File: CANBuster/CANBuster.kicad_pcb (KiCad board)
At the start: 2 copper layers, 100 x 100 mm, 182 parts, among them CON1 BARREL_JACK, J1 RJ45, J2 RJ45, J3 RJ12, P1 CONN_01X10, P10 CONN_02X04, P11 RS232-Programmer, P12 S88, P13 CONN_01X10, P14 CONN_01X10, P15 TRACK, P16 CONN_01X02, P17 USB_OTG, P18 CONN_01X03, P2 CONN_01X10, P3 CONN_01X03, P4 CONN_01X03, P5 CONN_01X03, P6 CONN_01X03, P7 CONN_01X02, P8 CONN_01X06, P9 CONN_01X04, Q1 BC547, Q2 BC547, SW1 SW_PUSH, SW2 SW_PUSH, U1 PIC18F45K80, U12 MCP2561, U2 MCP2561, U3 7805, U4 LTV-844, U5 LTV-844, U6 LTV-844, U7 LTV-844, U8 ISO1050, Y1 16MHz

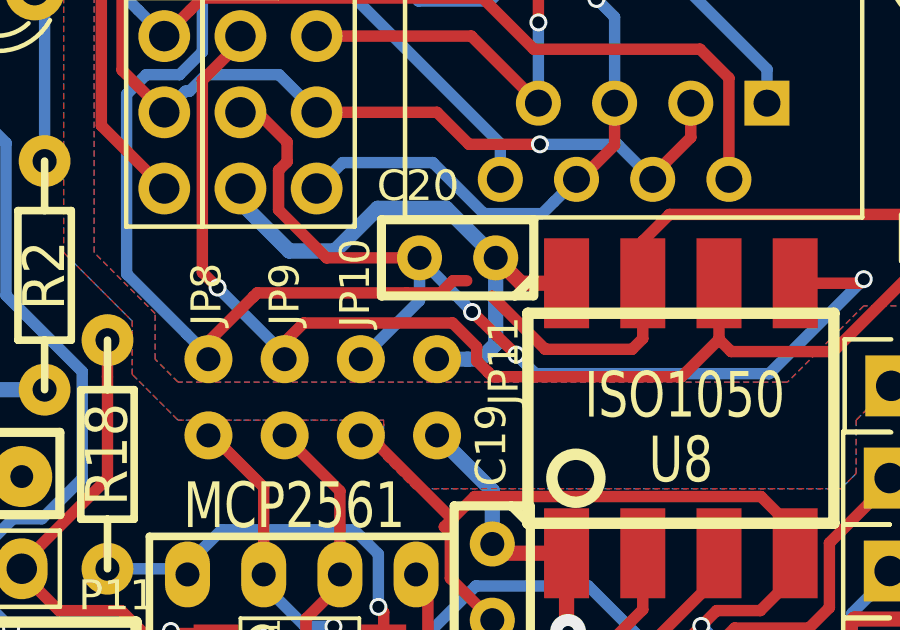
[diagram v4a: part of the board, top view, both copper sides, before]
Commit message: finish 5V option
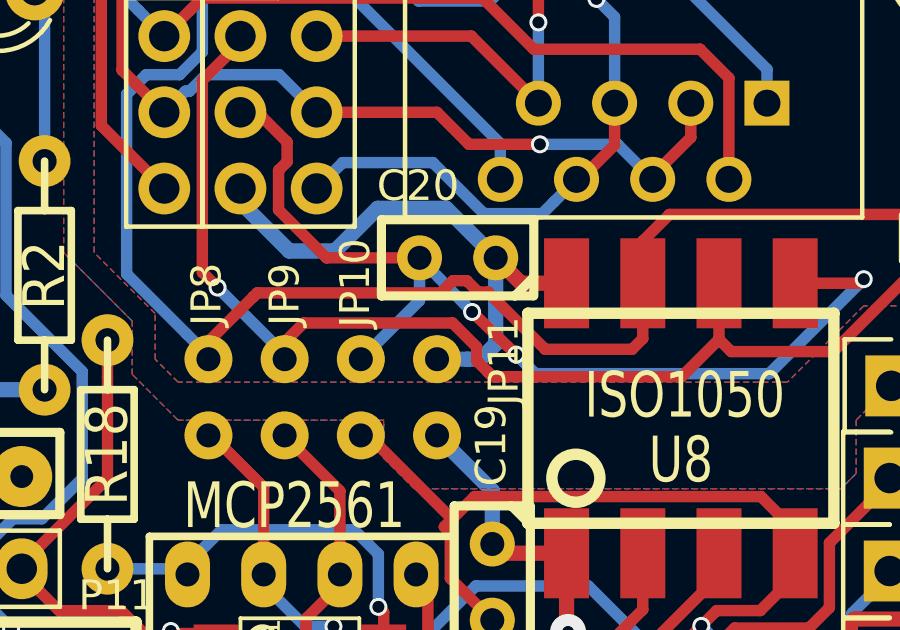
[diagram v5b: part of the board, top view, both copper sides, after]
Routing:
- net /CANH: track 46.3 -> 47.4 mm
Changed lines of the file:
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@@
-(kicad_pcb (version 4) (host pcbnew 4.0.2-4+6225~38~ubuntu14.04.1-stable)
+(kicad_pcb (version 4) (host pcbnew 4.0.1-stable)
   (general
     (links 463)
-    (no_connects 36)
-    (area 70.028999 35.052999 170.179001 135.203001)
+    (no_connects 0)
+    (area 69.215499 29.4545 181.99 144.85554)
     (thickness 1.6)
     (drawings 32)
-    (tracks 1756)
+    (tracks 1755)
     (zones 0)
     (modules 182)
@@
   (segment (start 157.6324 53.086) (end 157.226 52.6796) (width 0.381) (layer F.Cu) (net 36))
   (segment (start 157.226 52.6796) (end 157.226 50.8085) (width 0.381) (layer F.Cu) (net 36))
-  (segment (start 146.812 51.1302) (end 141.8336 51.1302) (width 0.381) (layer F.Cu) (net 37))
-  (segment (start 146.812 51.1302) (end 147.955 51.1302) (width 0.381) (layer F.Cu) (net 37))
-  (segment (start 148.3614 50.7238) (end 147.955 51.1302) (width 0.381) (layer F.Cu) (net 37))
   (segment (start 141.7066 51.2572) (end 141.8336 51.1302) (width 0.381) (layer F.Cu) (net 37))
   (segment (start 148.3614 50.7238) (end 148.8186 50.7238) (width 0.381) (layer F.Cu) (net 37))
-  (segment (start 149.6695 51.2445) (end 149.6441 51.2445) (width 0.381) (layer F.Cu) (net 37))
-  (segment (start 151.4348 53.0098) (end 149.6695 51.2445) (width 0.381) (layer F.Cu) (net 37))
-  (segment (start 154.686 50.8085) (end 154.686 52.6542) (width 0.381) (layer F.Cu) (net 37))
+  (segment (start 149.197671 51.102871) (end 149.527871 51.102871) (width 0.381) (layer F.Cu) (net 37))
+  (segment (start 141.8336 51.1302) (end 147.955 51.1302) (width 0.381) (layer F.Cu) (net 37))
+  (segment (start 149.527871 51.102871) (end 151.4348 53.0098) (width 0.381) (layer F.Cu) (net 37))
+  (segment (start 147.955 51.1302) (end 148.3614 50.7238) (width 0.381) (layer F.Cu) (net 37))
+  (segment (start 148.8186 50.7238) (end 149.197671 51.102871) (width 0.381) (layer F.Cu) (net 37))
+  (segment (start 151.4348 53.0098) (end 154.3304 53.0098) (width 0.381) (layer F.Cu) (net 37))
   (segment (start 154.3304 53.0098) (end 154.686 52.6542) (width 0.381) (layer F.Cu) (net 37))
-  (segment (start 151.4983 53.0098) (end 154.3304 53.0098) (width 0.381) (layer F.Cu) (net 37))
-  (segment (start 151.4983 53.0098) (end 151.4348 53.0098) (width 0.381) (layer F.Cu) (net 37))
+  (segment (start 154.686 52.6542) (end 154.686 50.8085) (width 0.381) (layer F.Cu) (net 37))
   (segment (start 140.2842 52.6796) (end 141.7066 51.2572) (width 0.381) (layer F.Cu) (net 37))
   (segment (start 141.7066 51.2572) (end 141.7193 51.2572) (width 0.381) (layer F.Cu) (net 37))
@@
   (segment (start 150.4696 53.1876) (end 148.9964 51.7652) (width 0.381) (layer F.Cu) (net 151))
   (via (at 148.9964 51.7652) (size 0.6) (drill 0.4) (layers F.Cu B.Cu) (net 151))
-  (segment (start 147.2438 49.9618) (end 148.9964 51.7652) (width 0.381) (layer B.Cu) (net 151) (status 400000))
+  (segment (start 147.2438 49.9618) (end 148.9964 51.7652) (width 0.381) (layer B.Cu) (net 151))
   (segment (start 151.0284 53.7464) (end 150.4696 53.1876) (width 0.381) (layer B.Cu) (net 151))
   (via (at 150.4696 53.1876) (size 0.6) (drill 0.4) (layers F.Cu B.Cu) (net 151))
@@
     (connect_pads (clearance 0.254))
     (min_thickness 0.254)
-    (fill (arc_segments 16) (thermal_gap 0.508) (thermal_bridge_width 0.508))
+    (fill yes (arc_segments 16) (thermal_gap 0.508) (thermal_bridge_width 0.508))
     (polygon
       (pts
@@
     (connect_pads (clearance 0.254))
     (min_thickness 0.254)
-    (fill (arc_segments 16) (thermal_gap 0.508) (thermal_bridge_width 0.508))
+    (fill yes (arc_segments 16) (thermal_gap 0.508) (thermal_bridge_width 0.508))
     (polygon
       (pts
@@
     (connect_pads (clearance 0.254))
     (min_thickness 0.254)
-    (fill (arc_segments 16) (thermal_gap 0.508) (thermal_bridge_width 0.508))
+    (fill yes (arc_segments 16) (thermal_gap 0.508) (thermal_bridge_width 0.508))
     (polygon
       (pts
@@
     (connect_pads (clearance 0.254))
     (min_thickness 0.254)
-    (fill (arc_segments 16) (thermal_gap 0.508) (thermal_bridge_width 0.508))
+    (fill yes (arc_segments 16) (thermal_gap 0.508) (thermal_bridge_width 0.508))
     (polygon
       (pts
@@
     (connect_pads (clearance 0.254))
     (min_thickness 0.254)
-    (fill (arc_segments 16) (thermal_gap 0.508) (thermal_bridge_width 0.508))
+    (fill yes (arc_segments 16) (thermal_gap 0.508) (thermal_bridge_width 0.508))
     (polygon
       (pts
@@
     (connect_pads (clearance 0.254))
     (min_thickness 0.254)
-    (fill (arc_segments 16) (thermal_gap 0.508) (thermal_bridge_width 0.508))
+    (fill yes (arc_segments 16) (thermal_gap 0.508) (thermal_bridge_width 0.508))
     (polygon
       (pts
@@
     (connect_pads (clearance 0.254))
     (min_thickness 0.254)
-    (fill (arc_segments 16) (thermal_gap 0.508) (thermal_bridge_width 0.508))
+    (fill yes (arc_segments 16) (thermal_gap 0.508) (thermal_bridge_width 0.508))
     (polygon
       (pts
@@
     (connect_pads (clearance 0.254))
     (min_thickness 0.254)
-    (fill (arc_segments 16) (thermal_gap 0.508) (thermal_bridge_width 0.508))
+    (fill yes (arc_segments 16) (thermal_gap 0.508) (thermal_bridge_width 0.508))
     (polygon
       (pts

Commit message: bump version
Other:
- board text added: "CANBuster v1.2 4/2016 Gerhard Bertelsmann"
- board text removed: "CANBuster v1.1 3/2016 Gerhard Bertelsmann"
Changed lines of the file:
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@@
-(kicad_pcb (version 4) (host pcbnew 4.0.1-stable)
+(kicad_pcb (version 4) (host pcbnew 4.0.2-4+6225~38~ubuntu14.04.1-stable)
   (general
     (links 463)
@@
     (effects (font (size 1.2 1.2) (thickness 0.2)))
   )
-  (gr_text "CANBuster v1.1 3/2016\nGerhard Bertelsmann" (at 153.289 127.889) (layer F.Cu)
+  (gr_text "CANBuster v1.2 4/2016\nGerhard Bertelsmann" (at 153.289 127.889) (layer F.Cu)
     (effects (font (size 1.2 1.2) (thickness 0.25)))
   )

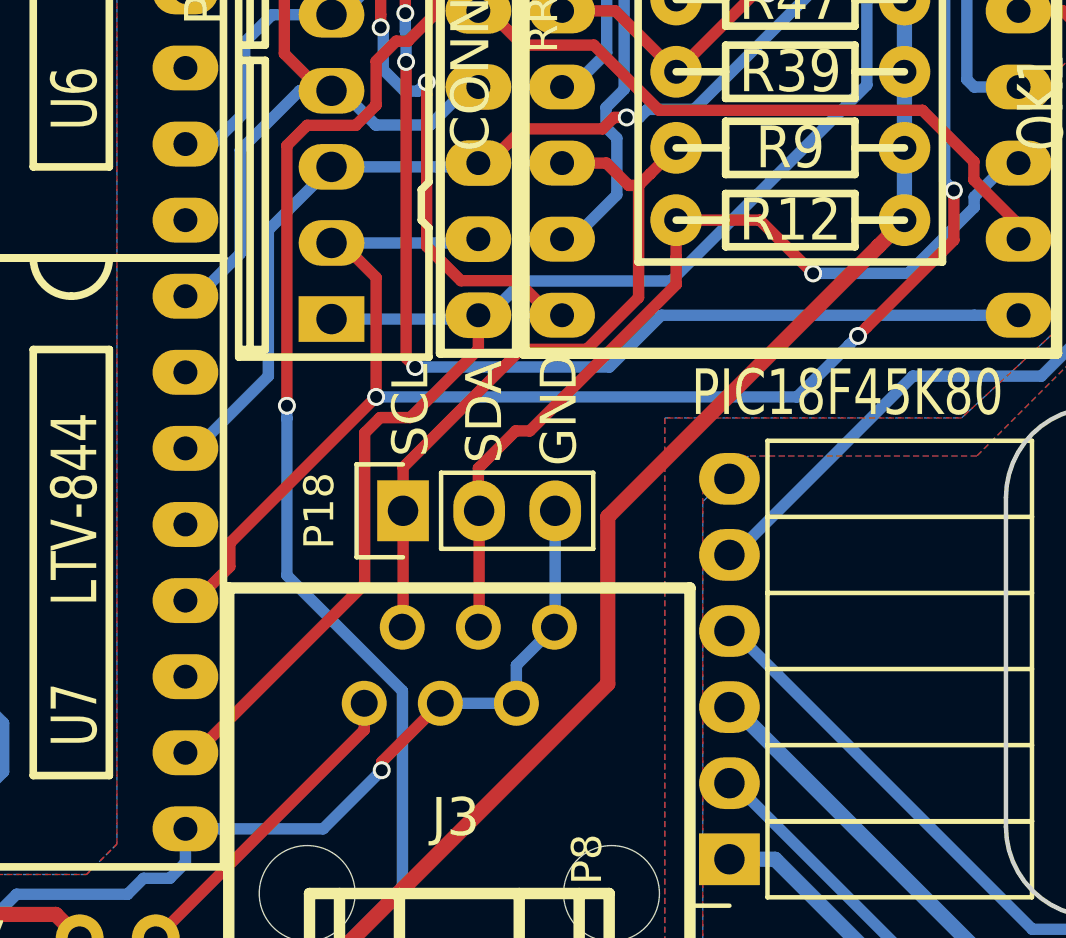
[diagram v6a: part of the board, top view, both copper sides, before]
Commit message: replace IIC 3 pin header with 4 pin - including Vdd
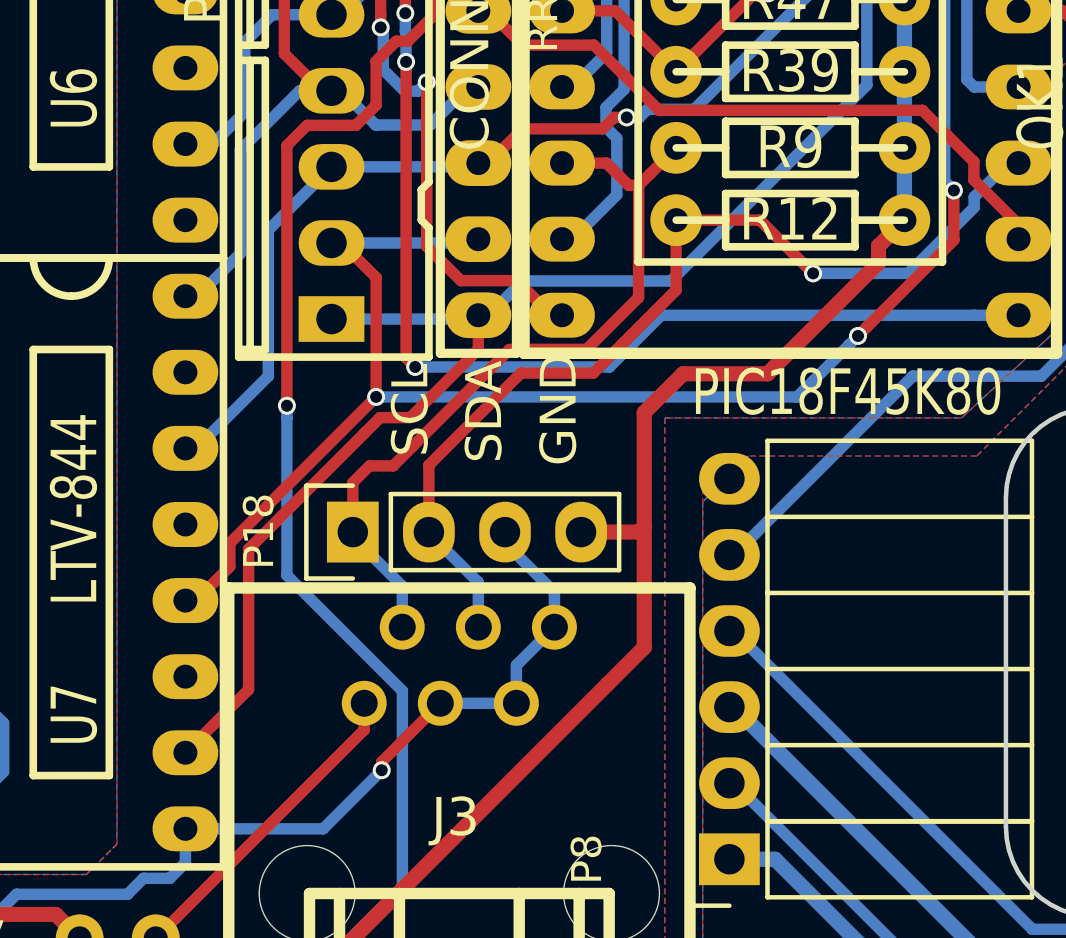
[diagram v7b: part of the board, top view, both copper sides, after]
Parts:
- P18: value CONN_01X03 -> CONN_01X04; footprint Pin_Headers:Pin_Header_Straight_1x03 -> Pin_Headers:Pin_Header_Straight_1x04
- moved P18 1.82 mm to (114.3, 118.9)
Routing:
- net VDD: track 333.7 -> 337.5 mm
- net /SDA: track 30.5 -> 33.0 mm
- net /SCL: track 23.9 -> 26.0 mm

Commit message: wip
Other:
- board text added: "CTS"
- board text added: "DTR"
- board text added: "RxD"
- board text added: "TxD"
- board text added: "Vcc"
- board text added: "Vdd"
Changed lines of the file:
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@@
-(kicad_pcb (version 4) (host pcbnew 4.0.2-4+6225~38~ubuntu14.04.1-stable)
+(kicad_pcb (version 4) (host pcbnew 4.0.1-stable)
   (general
     (links 464)
@@
     (area 70.028999 35.052999 170.179001 135.203001)
     (thickness 1.6)
-    (drawings 32)
+    (drawings 39)
     (tracks 1769)
     (zones 0)
@@
     )
   )
-  (gr_text GND (at 121.1834 114.7826 90) (layer F.SilkS)
+  (gr_text DTR (at 132.08 117.221) (layer F.SilkS)
     (effects (font (size 1.2 1.2) (thickness 0.2)))
   )
-  (gr_text SCL (at 116.2304 114.808 90) (layer F.SilkS)
+  (gr_text RxD (at 132.08 119.761) (layer F.SilkS)
     (effects (font (size 1.2 1.2) (thickness 0.2)))
   )
-  (gr_text SDA (at 118.6942 114.8588 90) (layer F.SilkS)
+  (gr_text TxD (at 132.08 122.301) (layer F.SilkS)
+    (effects (font (size 1.2 1.2) (thickness 0.2)))
+  )
+  (gr_text Vcc (at 132.08 124.841) (layer F.SilkS)
+    (effects (font (size 1.2 1.2) (thickness 0.2)))
+  )
+  (gr_text CTS (at 132.08 127.381) (layer F.SilkS)
+    (effects (font (size 1.2 1.2) (thickness 0.2)))
+  )
+  (gr_text GND (at 132.08 129.921) (layer F.SilkS)
+    (effects (font (size 1.2 1.2) (thickness 0.2)))
+  )
+  (gr_text Vdd (at 122.047 115.062 90) (layer F.SilkS)
+    (effects (font (size 1.2 1.2) (thickness 0.2)))
+  )
+  (gr_text GND (at 119.507 115.062 90) (layer F.SilkS)
+    (effects (font (size 1.2 1.2) (thickness 0.2)))
+  )
+  (gr_text SCL (at 114.173 115.062 90) (layer F.SilkS)
+    (effects (font (size 1.2 1.2) (thickness 0.2)))
+  )
+  (gr_text SDA (at 116.84 115.189 90) (layer F.SilkS)
     (effects (font (size 1.2 1.2) (thickness 0.2)))
   )
